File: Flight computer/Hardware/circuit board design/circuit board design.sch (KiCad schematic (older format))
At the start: 0 parts

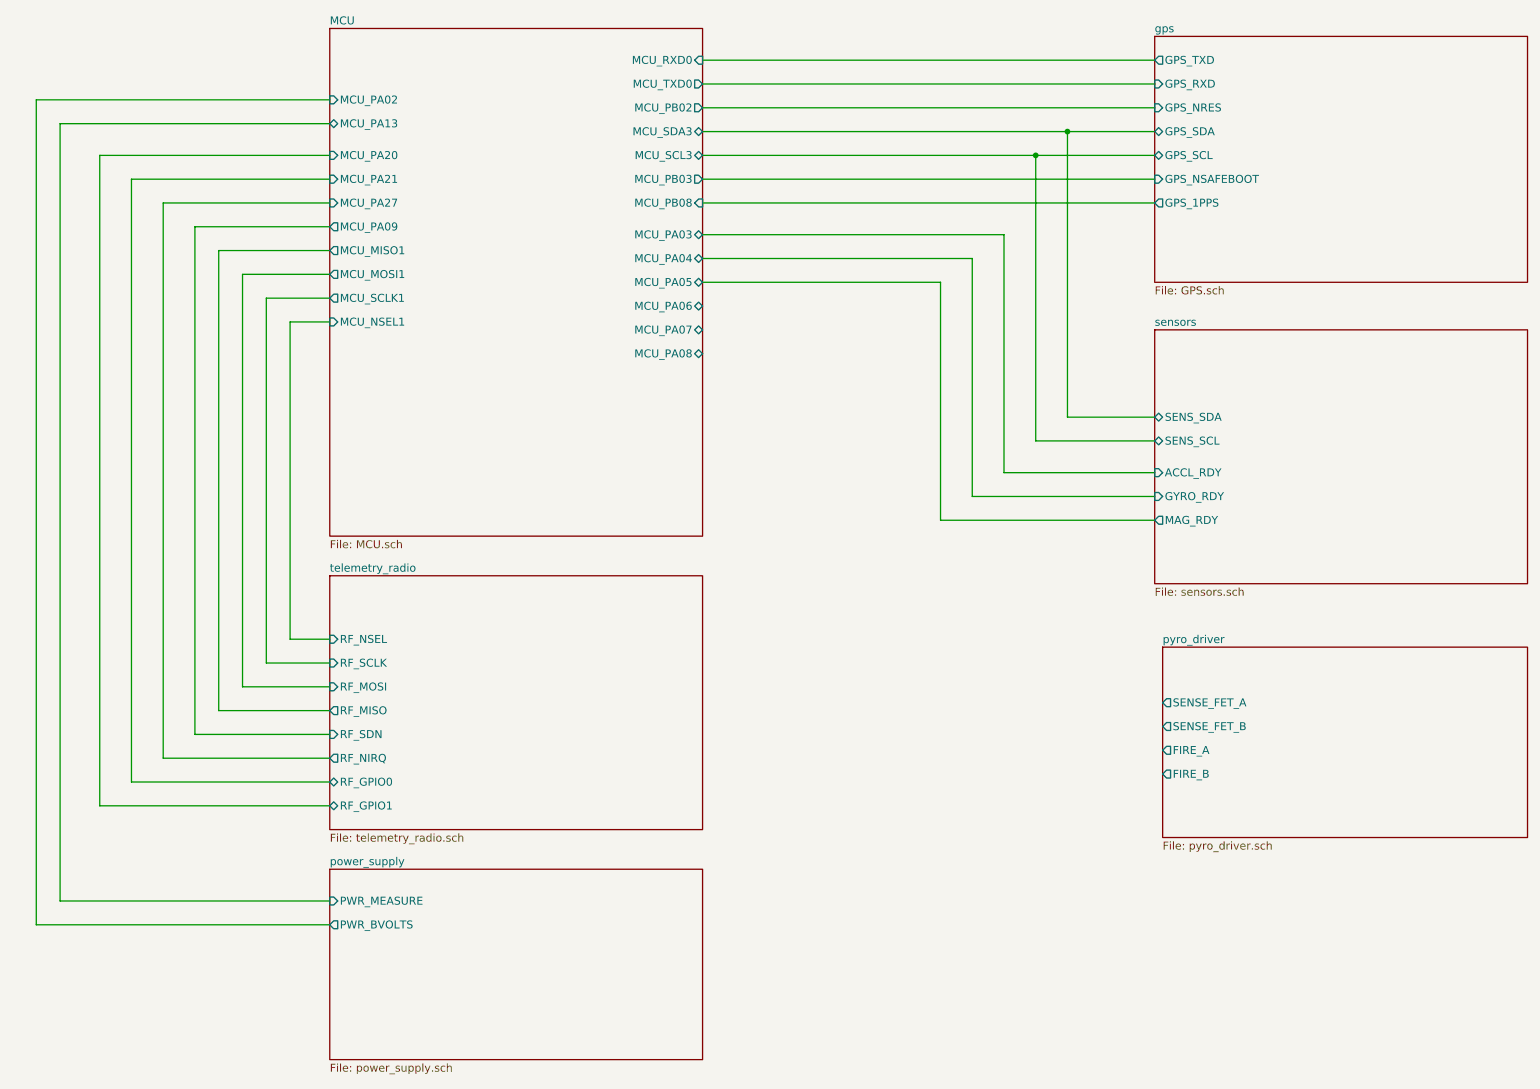
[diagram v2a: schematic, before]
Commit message: Wired up the FETs
-fixed the ERC error for the BMI088 symbol
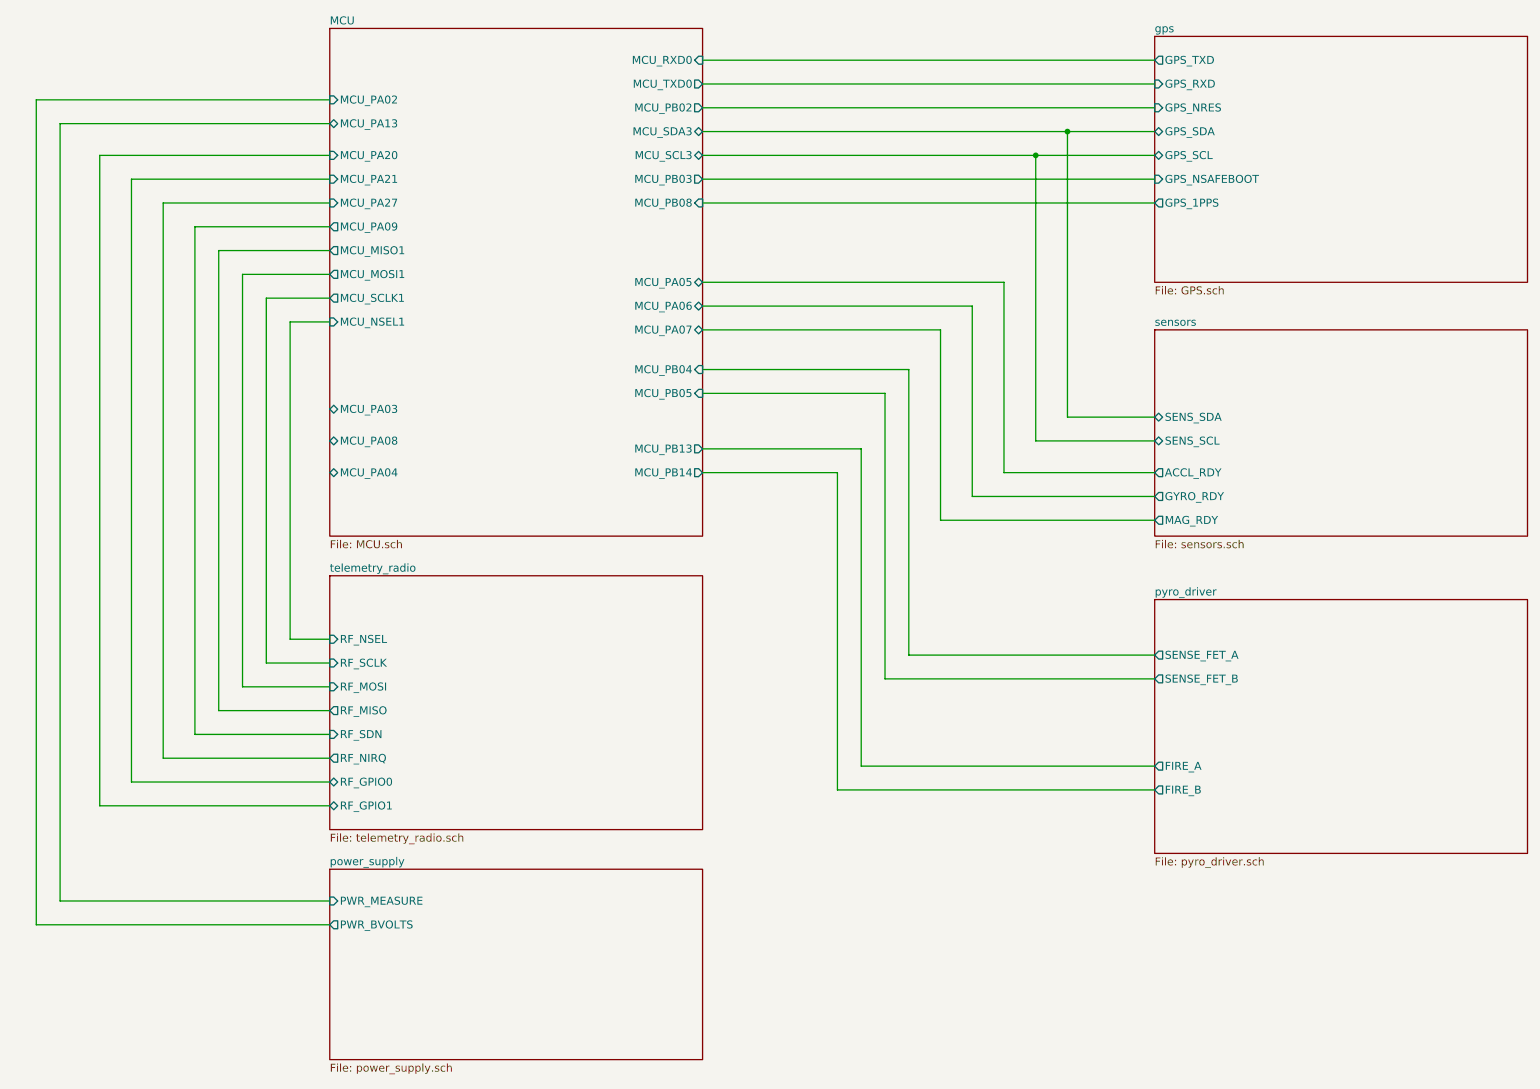
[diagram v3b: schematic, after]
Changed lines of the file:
@@
 $EndDescr
 $Sheet
-S 7900 3000 2350 1600
+S 7900 3000 2350 1300
 U 5D5B1586
 F0 "sensors" 50
@@
 F2 "SENS_SDA" B L 7900 3550 50
 F3 "SENS_SCL" B L 7900 3700 50
-F4 "ACCL_RDY" I L 7900 3900 50
-F5 "GYRO_RDY" I L 7900 4050 50
-F6 "MAG_RDY" O L 7900 4200 50
+F4 "MAG_RDY" O L 7900 4200 50
+F5 "ACCL_RDY" O L 7900 3900 50
+F6 "GYRO_RDY" O L 7900 4050 50
 $EndSheet
 $Sheet
@@
 	7150 1900 7900 1900
 $Sheet
-S 7950 5000 2300 1200
+S 7900 4700 2350 1600
 U 5D6468D5
 F0 "pyro_driver" 50
 F1 "pyro_driver.sch" 50
-F2 "SENSE_FET_A" O L 7950 5350 50
-F3 "FIRE_A" O L 7950 5650 50
-F4 "SENSE_FET_B" O L 7950 5500 50
-F5 "FIRE_B" O L 7950 5800 50
+F2 "SENSE_FET_A" O L 7900 5050 50
+F3 "FIRE_A" O L 7900 5750 50
+F4 "SENSE_FET_B" O L 7900 5200 50
+F5 "FIRE_B" O L 7900 5900 50
 $EndSheet
 Wire Wire Line
 	7900 3900 6950 3900
-Wire Wire Line
-	6950 3900 6950 2400
 $Sheet
 S 2700 6400 2350 1200
@@
 	7900 4050 6750 4050
 Wire Wire Line
-	6750 4050 6750 2550
-Wire Wire Line
 	1650 2200 2700 2200
 Wire Wire Line
@@
 	1850 2350 2700 2350
 Wire Wire Line
-	6750 2550 5050 2550
-Wire Wire Line
-	6950 2400 5050 2400
+	6750 2850 5050 2850
+Wire Wire Line
+	6950 2700 5050 2700
 Wire Wire Line
 	2700 1550 850  1550
@@
 F9 "MCU_RXD0" I R 5050 1300 50
 F10 "MCU_PA02" I L 2700 1550 50
-F11 "MCU_PA03" B R 5050 2400 50
-F12 "MCU_PA04" B R 5050 2550 50
-F13 "MCU_PA05" B R 5050 2700 50
-F14 "MCU_PA06" B R 5050 2850 50
-F15 "MCU_PA07" B R 5050 3000 50
-F16 "MCU_PA08" B R 5050 3150 50
-F17 "MCU_PA09" O L 2700 2350 50
-F18 "MCU_PA13" B L 2700 1700 50
-F19 "MCU_PB03" O R 5050 2050 50
-F20 "MCU_PB02" O R 5050 1600 50
-F21 "MCU_PB08" I R 5050 2200 50
-F22 "MCU_PA20" I L 2700 1900 50
-F23 "MCU_PA21" I L 2700 2050 50
-F24 "MCU_PA27" I L 2700 2200 50
-$EndSheet
-Wire Wire Line
-	5050 2700 6550 2700
-Wire Wire Line
-	6550 2700 6550 4200
+F11 "MCU_PA05" B R 5050 2700 50
+F12 "MCU_PA06" B R 5050 2850 50
+F13 "MCU_PA07" B R 5050 3000 50
+F14 "MCU_PA09" O L 2700 2350 50
+F15 "MCU_PA13" B L 2700 1700 50
+F16 "MCU_PB03" O R 5050 2050 50
+F17 "MCU_PB02" O R 5050 1600 50
+F18 "MCU_PB08" I R 5050 2200 50
+F19 "MCU_PA20" I L 2700 1900 50
+F20 "MCU_PA21" I L 2700 2050 50
+F21 "MCU_PA27" I L 2700 2200 50
+F22 "MCU_PA03" B L 2700 3500 50
+F23 "MCU_PA04" B L 2700 3900 50
+F24 "MCU_PA08" B L 2700 3700 50
+F25 "MCU_PB04" I R 5050 3250 50
+F26 "MCU_PB05" I R 5050 3400 50
+F27 "MCU_PB13" O R 5050 3750 50
+F28 "MCU_PB14" O R 5050 3900 50
+$EndSheet
+Wire Wire Line
+	5050 3000 6550 3000
+Wire Wire Line
+	6550 3000 6550 4200
+Wire Wire Line
+	6750 4050 6750 2850
+Wire Wire Line
+	6950 3900 6950 2700
 Wire Wire Line
 	6550 4200 7900 4200
+Wire Wire Line
+	7900 5050 6350 5050
+Wire Wire Line
+	6350 5050 6350 3250
+Wire Wire Line
+	6350 3250 5050 3250
+Wire Wire Line
+	5050 3400 6200 3400
+Wire Wire Line
+	6200 3400 6200 5200
+Wire Wire Line
+	6200 5200 7900 5200
+Wire Wire Line
+	7900 5750 6050 5750
+Wire Wire Line
+	6050 5750 6050 3750
+Wire Wire Line
+	6050 3750 5050 3750
+Wire Wire Line
+	5050 3900 5900 3900
+Wire Wire Line
+	5900 3900 5900 5900
+Wire Wire Line
+	5900 5900 7900 5900
 $EndSCHEMATC

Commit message: connected 4 channels of pyro drivers
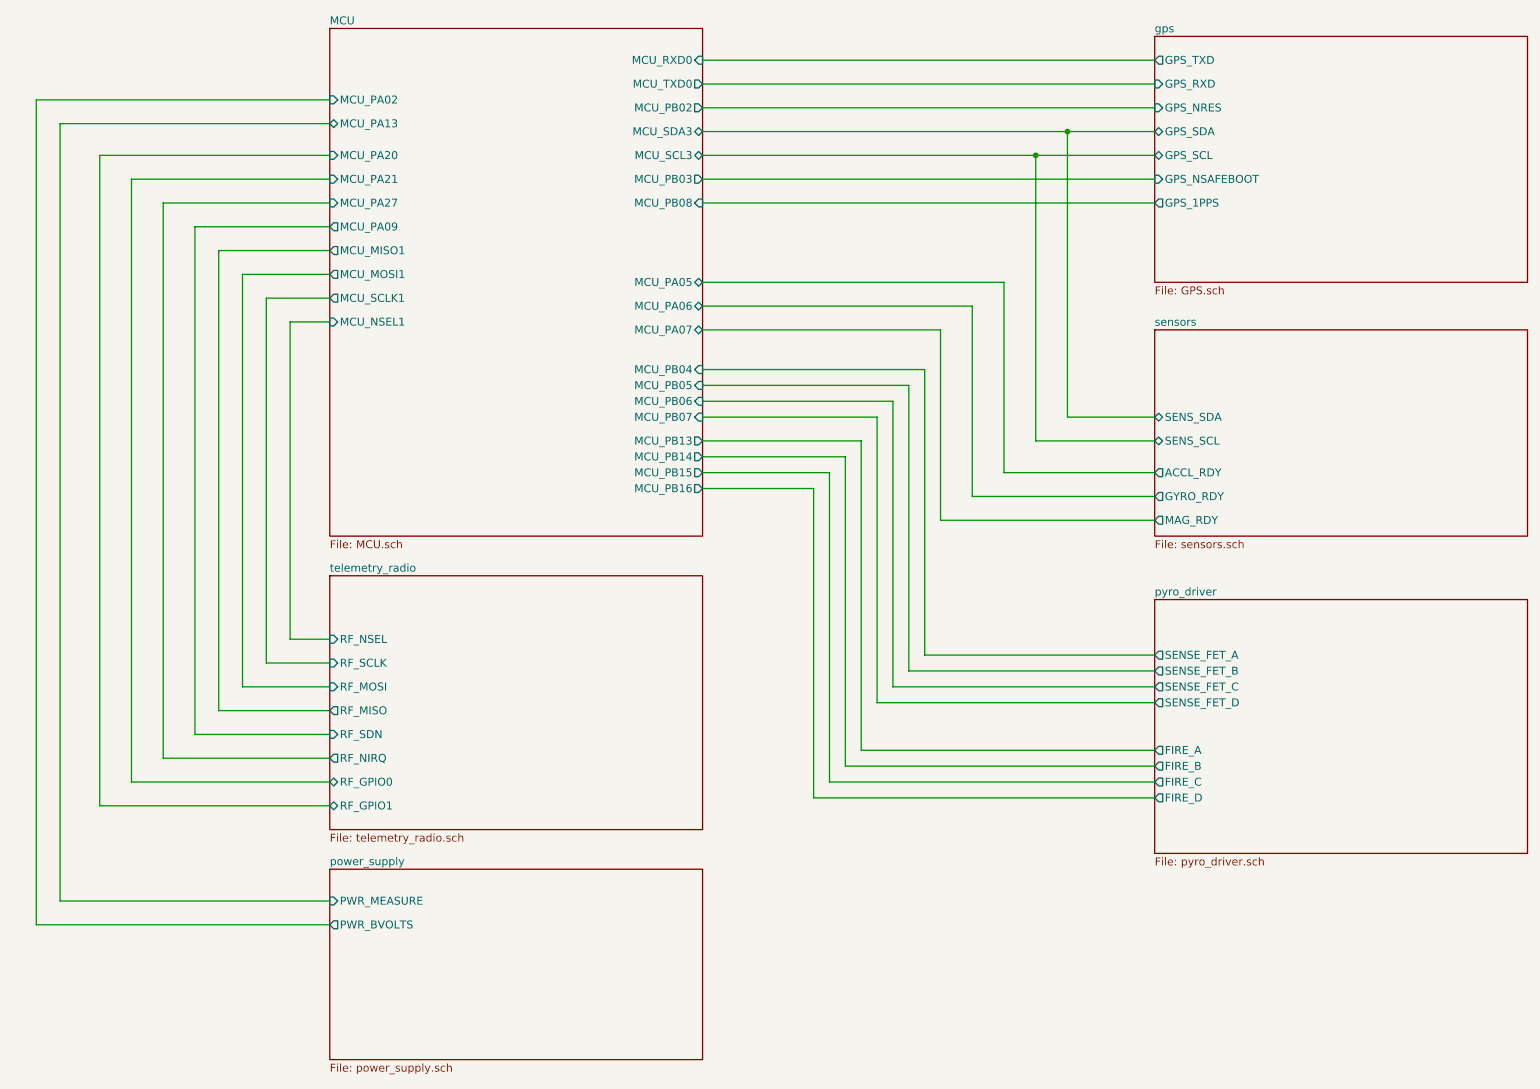
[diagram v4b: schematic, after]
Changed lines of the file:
@@
 Wire Wire Line
 	7150 1900 7900 1900
-$Sheet
-S 7900 4700 2350 1600
-U 5D6468D5
-F0 "pyro_driver" 50
-F1 "pyro_driver.sch" 50
-F2 "SENSE_FET_A" O L 7900 5050 50
-F3 "FIRE_A" O L 7900 5750 50
-F4 "SENSE_FET_B" O L 7900 5200 50
-F5 "FIRE_B" O L 7900 5900 50
-$EndSheet
 Wire Wire Line
 	7900 3900 6950 3900
@@
 F20 "MCU_PA21" I L 2700 2050 50
 F21 "MCU_PA27" I L 2700 2200 50
-F22 "MCU_PA03" B L 2700 3500 50
-F23 "MCU_PA04" B L 2700 3900 50
-F24 "MCU_PA08" B L 2700 3700 50
-F25 "MCU_PB04" I R 5050 3250 50
-F26 "MCU_PB05" I R 5050 3400 50
-F27 "MCU_PB13" O R 5050 3750 50
-F28 "MCU_PB14" O R 5050 3900 50
+F22 "MCU_PB04" I R 5050 3250 50
+F23 "MCU_PB05" I R 5050 3350 50
+F24 "MCU_PB13" O R 5050 3700 50
+F25 "MCU_PB14" O R 5050 3800 50
+F26 "MCU_PB06" I R 5050 3450 50
+F27 "MCU_PB07" I R 5050 3550 50
+F28 "MCU_PB15" O R 5050 3900 50
+F29 "MCU_PB16" O R 5050 4000 50
 $EndSheet
 Wire Wire Line
@@
 	6550 4200 7900 4200
 Wire Wire Line
-	7900 5050 6350 5050
-Wire Wire Line
-	6350 5050 6350 3250
-Wire Wire Line
-	6350 3250 5050 3250
-Wire Wire Line
-	5050 3400 6200 3400
-Wire Wire Line
-	6200 3400 6200 5200
-Wire Wire Line
-	6200 5200 7900 5200
-Wire Wire Line
-	7900 5750 6050 5750
-Wire Wire Line
-	6050 5750 6050 3750
-Wire Wire Line
-	6050 3750 5050 3750
-Wire Wire Line
-	5050 3900 5900 3900
-Wire Wire Line
-	5900 3900 5900 5900
-Wire Wire Line
-	5900 5900 7900 5900
+	6450 3250 6450 5050
+Wire Wire Line
+	6450 5050 7900 5050
+Wire Wire Line
+	7900 5150 6350 5150
+Wire Wire Line
+	6350 5150 6350 3350
+Wire Wire Line
+	6350 3350 5050 3350
+Wire Wire Line
+	5050 3250 6450 3250
+Wire Wire Line
+	5050 3450 6250 3450
+Wire Wire Line
+	6250 3450 6250 5250
+Wire Wire Line
+	6150 5350 6150 3550
+Wire Wire Line
+	6150 3550 5050 3550
+Wire Wire Line
+	5050 3700 6050 3700
+Wire Wire Line
+	6050 3700 6050 5650
+Wire Wire Line
+	5950 5750 5950 3800
+Wire Wire Line
+	5950 3800 5050 3800
+Wire Wire Line
+	5050 3900 5850 3900
+Wire Wire Line
+	5850 3900 5850 5850
+Wire Wire Line
+	5750 5950 5750 4000
+Wire Wire Line
+	5750 4000 5050 4000
+Wire Wire Line
+	7900 5950 5750 5950
+Wire Wire Line
+	5850 5850 7900 5850
+Wire Wire Line
+	7900 5750 5950 5750
+Wire Wire Line
+	6050 5650 7900 5650
+Wire Wire Line
+	7900 5350 6150 5350
+Wire Wire Line
+	6250 5250 7900 5250
+$Sheet
+S 7900 4700 2350 1600
+U 5D6468D5
+F0 "pyro_driver" 50
+F1 "pyro_driver.sch" 50
+F2 "SENSE_FET_A" O L 7900 5050 50
+F3 "FIRE_A" O L 7900 5650 50
+F4 "SENSE_FET_B" O L 7900 5150 50
+F5 "FIRE_B" O L 7900 5750 50
+F6 "SENSE_FET_C" O L 7900 5250 50
+F7 "FIRE_C" O L 7900 5850 50
+F8 "SENSE_FET_D" O L 7900 5350 50
+F9 "FIRE_D" O L 7900 5950 50
+$EndSheet
 $EndSCHEMATC
